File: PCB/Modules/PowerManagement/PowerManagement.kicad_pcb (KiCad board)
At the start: 2 copper layers, 29 x 59 mm, 29 parts, among them J1 USB, J2 BUS, J3 In, J4 PWR, J5 BATT, J6 BUTT, U1 MP2723A, U2 TPS61032

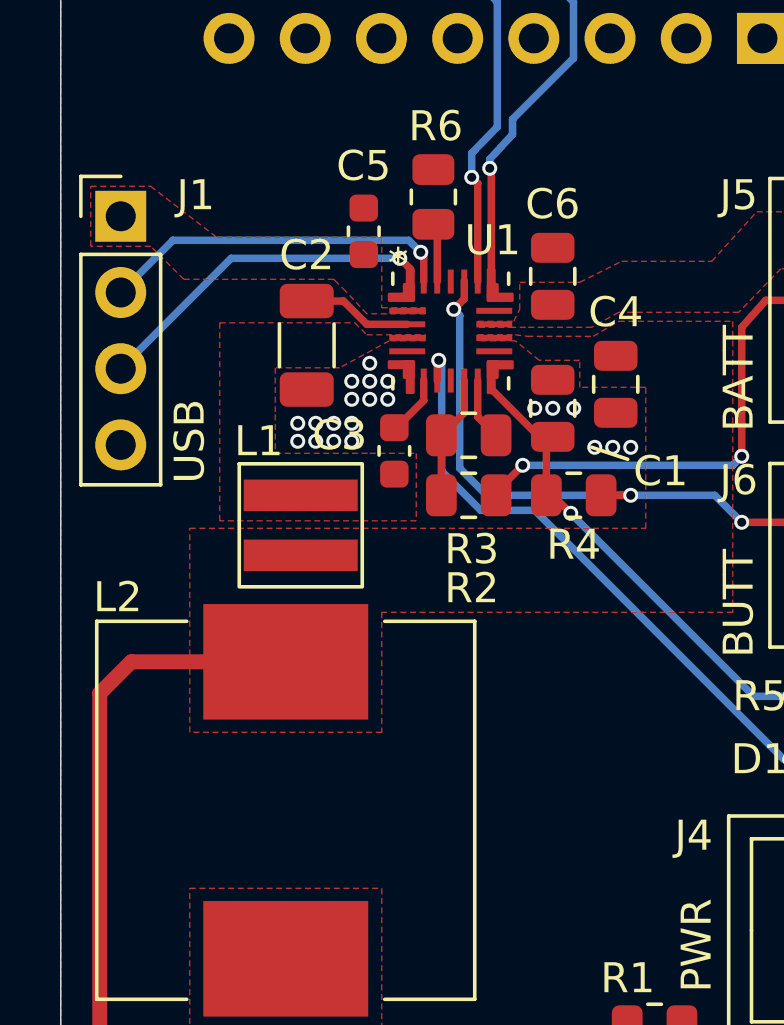
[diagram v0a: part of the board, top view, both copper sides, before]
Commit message: Convert all KiCad to 6.0, clean up libraries, remove files that shouldn't be committed.
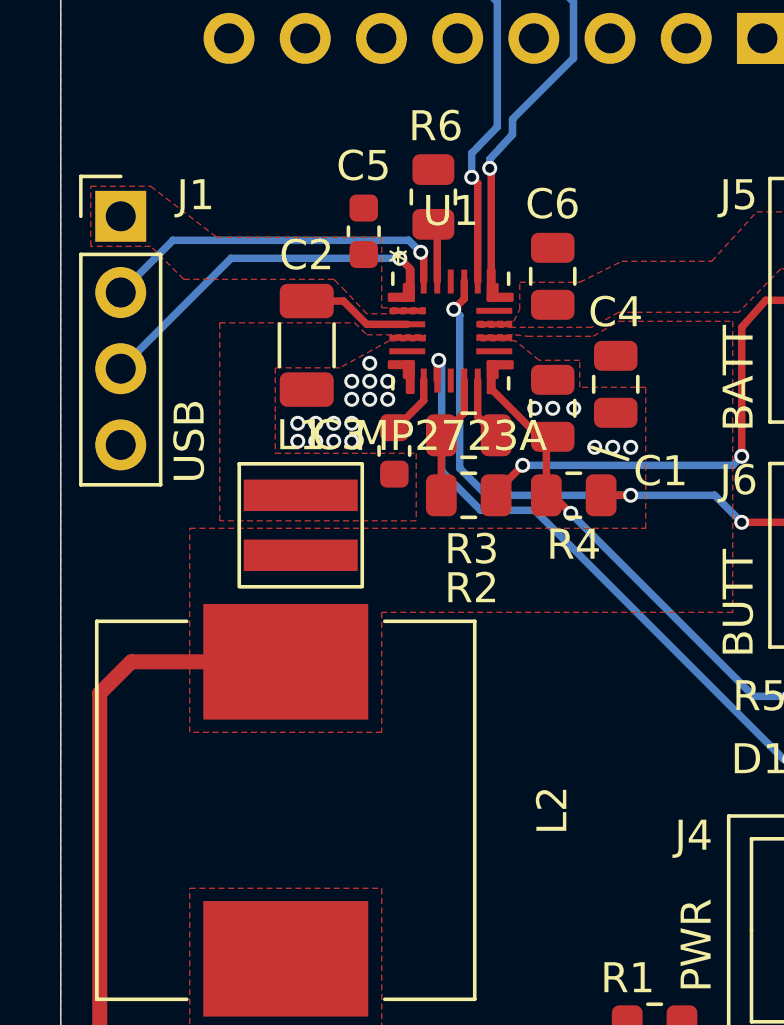
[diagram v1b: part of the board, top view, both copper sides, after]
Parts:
- J3: footprint Custom:PinHeader_2x08_P2.54mm_Vertical-Centered -> KTANE:PinHeader_2x08_P2.54mm_Vertical-Centered
- L1: footprint footprints:PA5001 -> KTANE:PA5001
- L2: footprint footprints:DR124 -> KTANE:DR124
- U1: footprint footprints:MP2723AGQC-0000-P -> KTANE:MP2723AGQC-0000-P
